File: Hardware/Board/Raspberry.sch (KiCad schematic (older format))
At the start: 5 parts

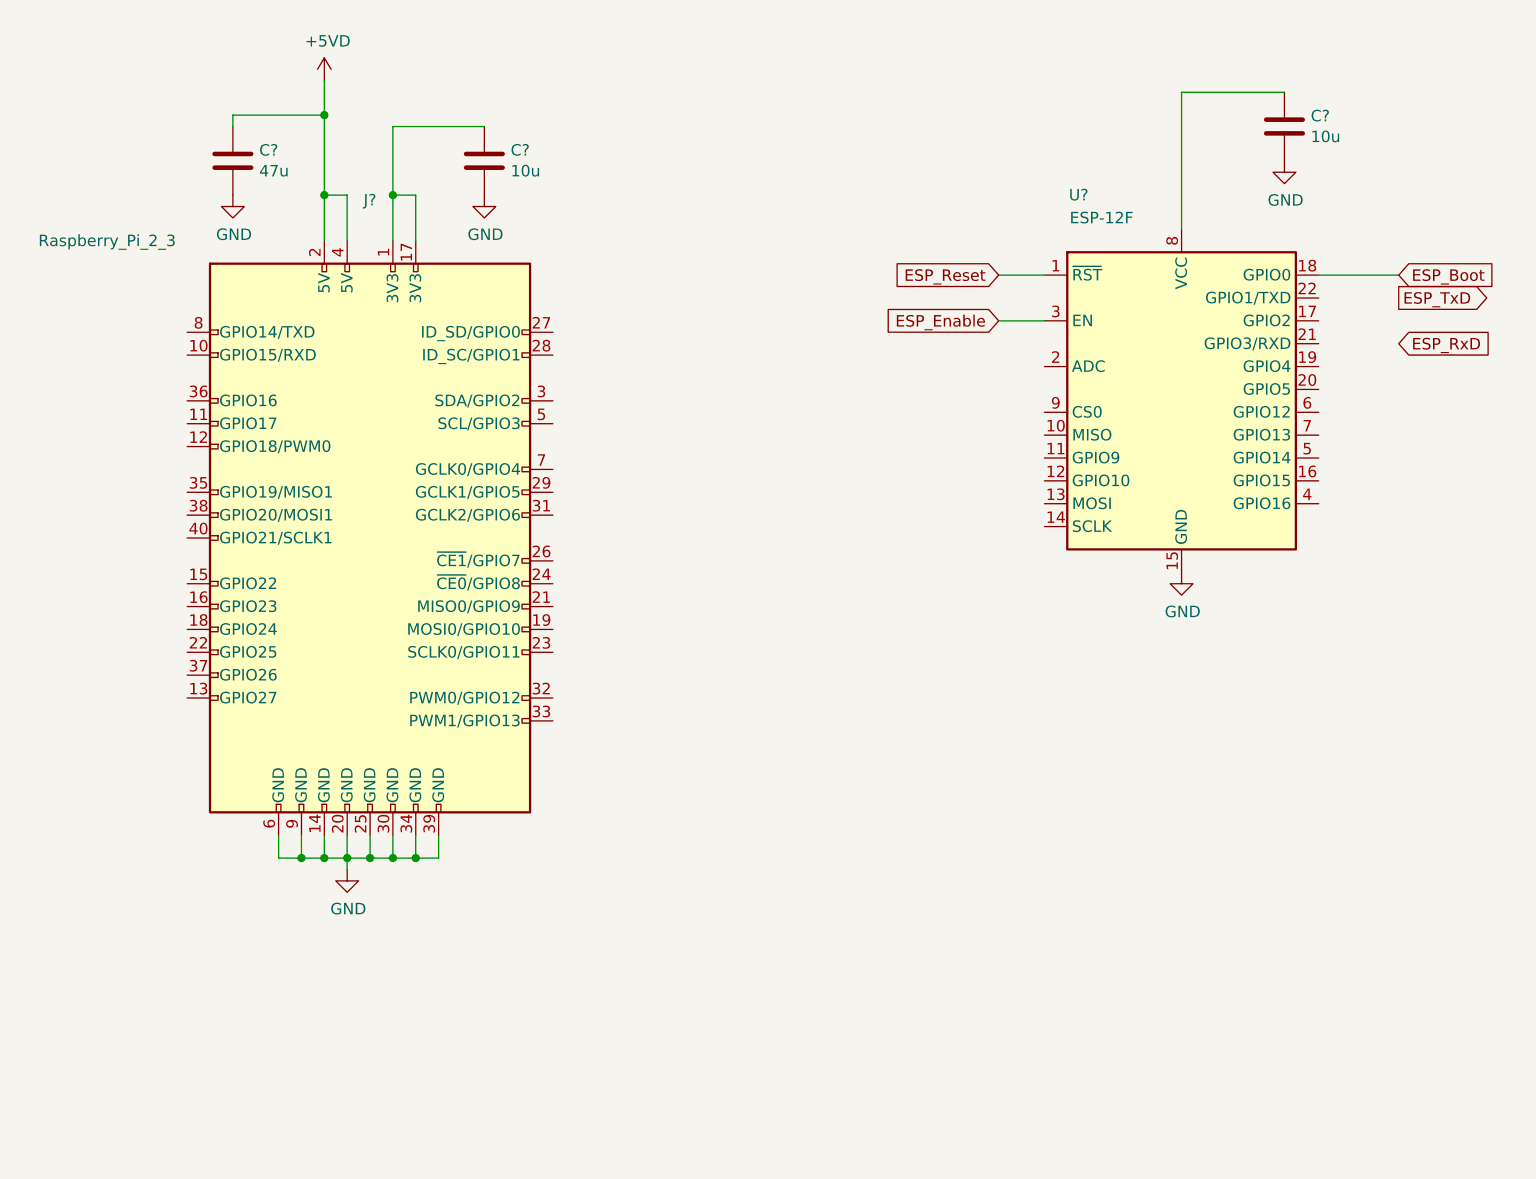
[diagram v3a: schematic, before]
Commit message: Netzliste und Board erstellt, hier sind noch Fehler im Bereich Footprints, BLE Modul nRF8001 hinzugefügt, erste Anschlussklemmen zugefügt
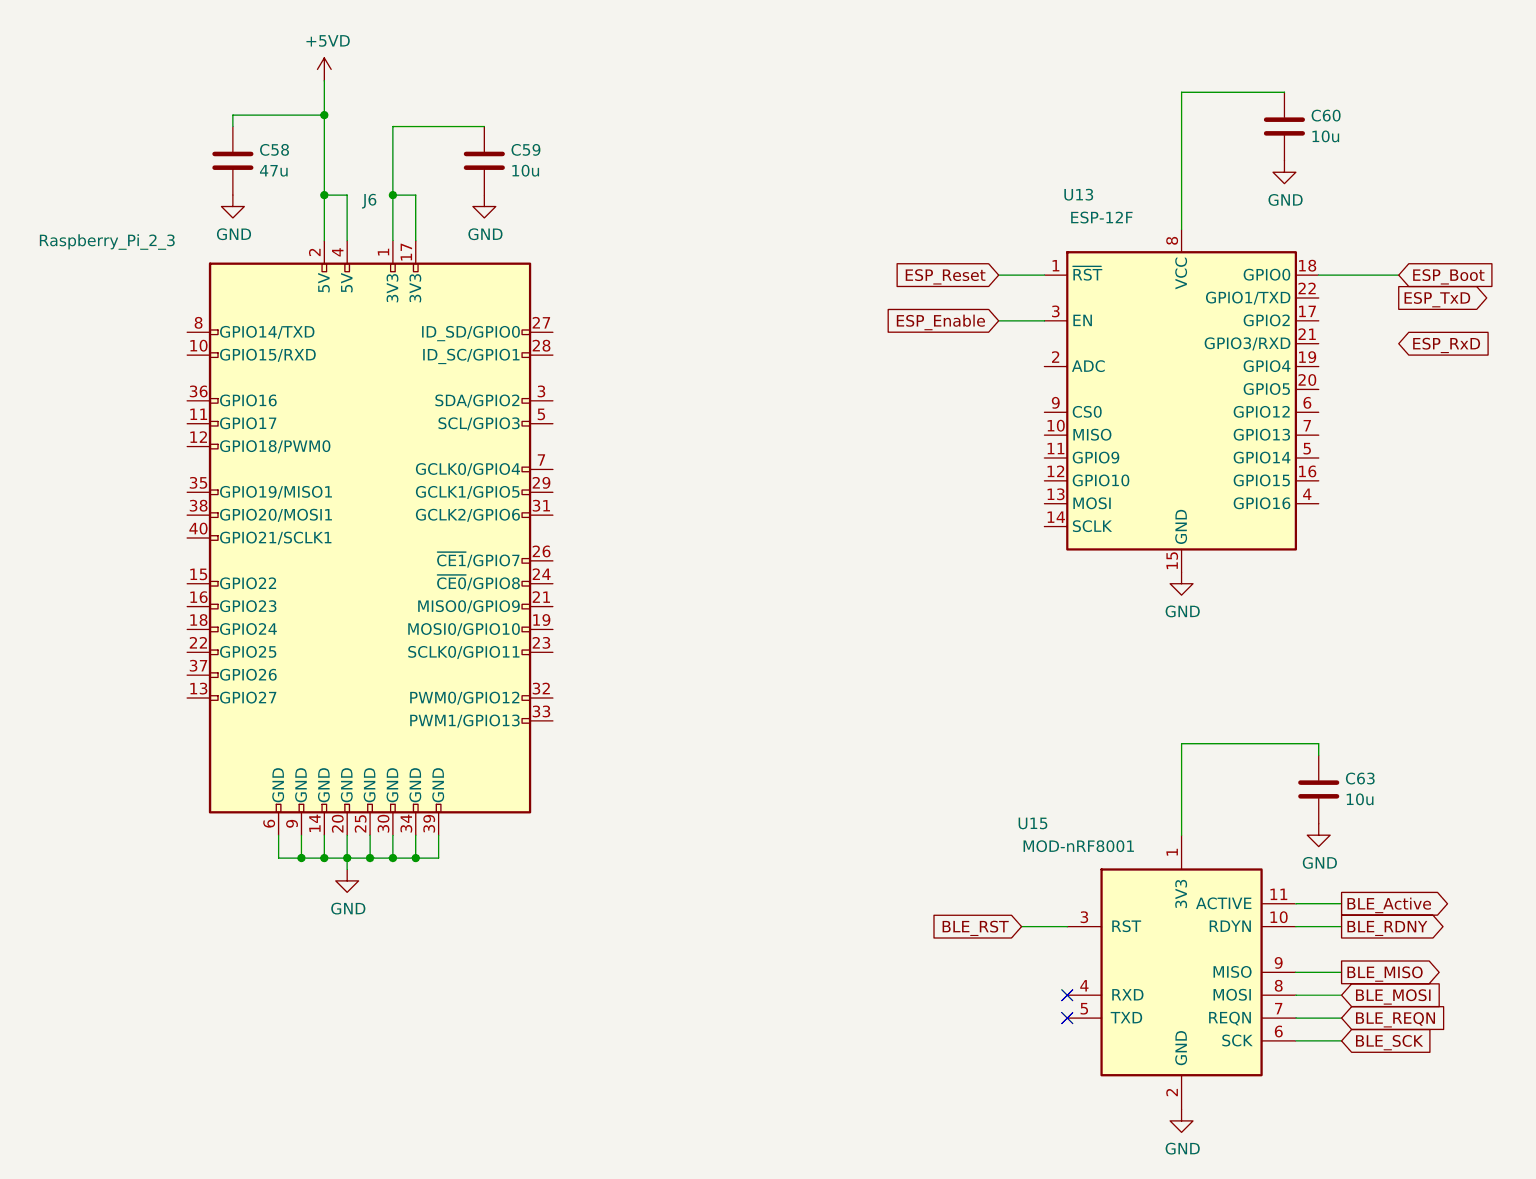
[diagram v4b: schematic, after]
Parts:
- added C63: 10u, Capacitor_SMD:C_1210_3225Metric, symbol Device:C
- added U15: MOD-nRF8001, RF_Module:MOD-nRF8001, symbol RF_Bluetooth:MOD-nRF8001
- C58, C59, C60: renamed from C?; footprint (none) -> Capacitor_SMD:C_1210_3225Metric
- J6: renamed from J?; footprint (none) -> Connector_IDC:IDC-Header_2x20_P2.54mm_Vertical
- gave numbers to parts that had none: 1
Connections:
- net GND: now also C63.2, U15.2 (GND)
- new net: C63.1, U15.1 (3V3)
- new net BLE_Active: U15.11 (ACTIVE)
- new net BLE_MISO: U15.9 (MISO)
- new net BLE_MOSI: U15.8 (MOSI)
- new net BLE_RDNY: U15.10 (RDYN)
- new net BLE_REQN: U15.7 (REQN)
- new net BLE_RST: U15.3 (RST)
- new net BLE_SCK: U15.6 (SCK)
- no-connect marks 0 -> 2
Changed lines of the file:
@@
 $EndDescr
 $Comp
-L Connector:Raspberry_Pi_2_3 J?
+L Connector:Raspberry_Pi_2_3 J6
 U 1 1 5C8BC8C5
 P 4400 3300
-F 0 "J?" H 4400 4778 50  0000 C CNN
+F 0 "J6" H 4400 4778 50  0000 C CNN
 F 1 "Raspberry_Pi_2_3" H 3250 4600 50  0000 C CNN
-F 2 "" H 4400 3300 50  0001 C CNN
+F 2 "Connector_IDC:IDC-Header_2x20_P2.54mm_Vertical" H 4400 3300 50  0001 C CNN
 F 3 "https://www.raspberrypi.org/documentation/hardware/raspberrypi/schematics/rpi_SCH_3bplus_1p0_reduced.pdf" H 4400 3300 50  0001 C CNN
 	1    4400 3300
@@
 $EndComp
 $Comp
-L power:GND #PWR?
+L power:GND #PWR0229
 U 1 1 5CC01696
 P 4300 4750
-F 0 "#PWR?" H 4300 4500 50  0001 C CNN
+F 0 "#PWR0229" H 4300 4500 50  0001 C CNN
 F 1 "GND" H 4305 4577 50  0000 C CNN
 F 2 "" H 4300 4750 50  0001 C CNN
@@
 	4600 4700 4500 4700
 $Comp
-L power:+5VD #PWR?
+L power:+5VD #PWR0230
 U 1 1 5CC0193E
 P 4200 1300
-F 0 "#PWR?" H 4200 1150 50  0001 C CNN
+F 0 "#PWR0230" H 4200 1150 50  0001 C CNN
 F 1 "+5VD" H 4215 1473 50  0000 C CNN
 F 2 "" H 4200 1300 50  0001 C CNN
@@
 $EndComp
 $Comp
-L Device:C C?
+L Device:C C58
 U 1 1 5CC01965
 P 3800 1650
-F 0 "C?" H 3915 1696 50  0000 L CNN
+F 0 "C58" H 3915 1696 50  0000 L CNN
 F 1 "47u" H 3915 1605 50  0000 L CNN
-F 2 "" H 3838 1500 50  0001 C CNN
+F 2 "Capacitor_SMD:C_1210_3225Metric" H 3838 1500 50  0001 C CNN
 F 3 "~" H 3800 1650 50  0001 C CNN
 	1    3800 1650
@@
 $EndComp
 $Comp
-L Device:C C?
+L Device:C C59
 U 1 1 5CC019EB
 P 4900 1650
-F 0 "C?" H 5015 1696 50  0000 L CNN
+F 0 "C59" H 5015 1696 50  0000 L CNN
 F 1 "10u" H 5015 1605 50  0000 L CNN
-F 2 "" H 4938 1500 50  0001 C CNN
+F 2 "Capacitor_SMD:C_1210_3225Metric" H 4938 1500 50  0001 C CNN
 F 3 "~" H 4900 1650 50  0001 C CNN
 	1    4900 1650
@@
 $EndComp
 $Comp
-L power:GND #PWR?
+L power:GND #PWR0231
 U 1 1 5CC01A3B
 P 3800 1800
-F 0 "#PWR?" H 3800 1550 50  0001 C CNN
+F 0 "#PWR0231" H 3800 1550 50  0001 C CNN
 F 1 "GND" H 3805 1627 50  0000 C CNN
 F 2 "" H 3800 1800 50  0001 C CNN
@@
 $EndComp
 $Comp
-L power:GND #PWR?
+L power:GND #PWR0232
 U 1 1 5CC01B10
 P 4900 1800
-F 0 "#PWR?" H 4900 1550 50  0001 C CNN
+F 0 "#PWR0232" H 4900 1550 50  0001 C CNN
 F 1 "GND" H 4905 1627 50  0000 C CNN
 F 2 "" H 4900 1800 50  0001 C CNN
@@
 	4200 1450 4200 1300
 $Comp
-L RF_Module:ESP-12F U?
+L RF_Module:ESP-12F U13
 U 1 1 5CAB8BB3
 P 7950 2750
-F 0 "U?" H 7500 3700 50  0000 C CNN
+F 0 "U13" H 7500 3700 50  0000 C CNN
 F 1 "ESP-12F" H 7600 3600 50  0000 C CNN
 F 2 "RF_Module:ESP-12E" H 7950 2750 50  0001 C CNN
@@
 ESP_Enable
 $Comp
-L Device:C C?
+L Device:C C60
 U 1 1 5CB2F4A7
 P 8400 1500
-F 0 "C?" H 8515 1546 50  0000 L CNN
+F 0 "C60" H 8515 1546 50  0000 L CNN
 F 1 "10u" H 8515 1455 50  0000 L CNN
-F 2 "" H 8438 1350 50  0001 C CNN
+F 2 "Capacitor_SMD:C_1210_3225Metric" H 8438 1350 50  0001 C CNN
 F 3 "~" H 8400 1500 50  0001 C CNN
 	1    8400 1500
@@
 $EndComp
 $Comp
-L power:GND #PWR?
+L power:GND #PWR0233
 U 1 1 5CB2F4AE
 P 8400 1650
-F 0 "#PWR?" H 8400 1400 50  0001 C CNN
+F 0 "#PWR0233" H 8400 1400 50  0001 C CNN
 F 1 "GND" H 8405 1477 50  0000 C CNN
 F 2 "" H 8400 1650 50  0001 C CNN
@@
 $EndComp
 $Comp
-L power:GND #PWR?
+L power:GND #PWR0234
 U 1 1 5CB2F86B
 P 7950 3450
-F 0 "#PWR?" H 7950 3200 50  0001 C CNN
+F 0 "#PWR0234" H 7950 3200 50  0001 C CNN
 F 1 "GND" H 7955 3277 50  0000 C CNN
 F 2 "" H 7950 3450 50  0001 C CNN
@@
 Wire Wire Line
 	7950 1350 8400 1350
+$Comp
+L RF_Bluetooth:MOD-nRF8001 U15
+U 1 1 5CDFE053
+P 7950 5200
+F 0 "U15" H 7300 5850 50  0000 C CNN
+F 1 "MOD-nRF8001" H 7500 5750 50  0000 C CNN
+F 2 "RF_Module:MOD-nRF8001" H 8000 5250 50  0001 C CNN
+F 3 "https://www.olimex.com/Products/Modules/RF/MOD-nRF8001/" H 8000 5200 50  0001 C CNN
+	1    7950 5200
+	1    0    0    -1
+$EndComp
+Text GLabel 8650 5300 2    50   Input ~ 0
+BLE_MOSI
+Text GLabel 8650 5500 2    50   Input ~ 0
+BLE_SCK
+Text GLabel 8650 5200 2    50   Output ~ 0
+BLE_MISO
+$Comp
+L power:GND #PWR0249
+U 1 1 5CDFE14F
+P 7950 5800
+F 0 "#PWR0249" H 7950 5550 50  0001 C CNN
+F 1 "GND" H 7955 5627 50  0000 C CNN
+F 2 "" H 7950 5800 50  0001 C CNN
+F 3 "" H 7950 5800 50  0001 C CNN
+	1    7950 5800
+	1    0    0    -1
+$EndComp
+$Comp
+L Device:C C63
+U 1 1 5CDFE647
+P 8550 4400
+F 0 "C63" H 8665 4446 50  0000 L CNN
+F 1 "10u" H 8665 4355 50  0000 L CNN
+F 2 "Capacitor_SMD:C_1210_3225Metric" H 8588 4250 50  0001 C CNN
+F 3 "~" H 8550 4400 50  0001 C CNN
+	1    8550 4400
+	1    0    0    -1
+$EndComp
+$Comp
+L power:GND #PWR0250
+U 1 1 5CDFE64E
+P 8550 4550
+F 0 "#PWR0250" H 8550 4300 50  0001 C CNN
+F 1 "GND" H 8555 4377 50  0000 C CNN
+F 2 "" H 8550 4550 50  0001 C CNN
+F 3 "" H 8550 4550 50  0001 C CNN
+	1    8550 4550
+	1    0    0    -1
+$EndComp
+Wire Wire Line
+	8550 4250 8550 4200
+Wire Wire Line
+	8550 4200 7950 4200
+Wire Wire Line
+	7950 4200 7950 4600
+NoConn ~ 7450 5300
+NoConn ~ 7450 5400
+Text GLabel 8650 5400 2    50   Input ~ 0
+BLE_REQN
+Text GLabel 8650 5000 2    50   Output ~ 0
+BLE_RDNY
+Text GLabel 8650 4900 2    50   Output ~ 0
+BLE_Active
+Text GLabel 7250 5000 0    50   Input ~ 0
+BLE_RST
+Wire Wire Line
+	7250 5000 7450 5000
+Wire Wire Line
+	8450 4900 8650 4900
+Wire Wire Line
+	8450 5000 8650 5000
+Wire Wire Line
+	8450 5200 8650 5200
+Wire Wire Line
+	8450 5300 8650 5300
+Wire Wire Line
+	8450 5400 8650 5400
+Wire Wire Line
+	8450 5500 8650 5500
 $EndSCHEMATC

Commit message: Eine Menge Arbeit auf der GPN, fast fertig im Schaltplan.
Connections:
- net UART4_TX: now reaches J6.10 (GPIO15/RXD)
- net Rasp_Shutdown: now reaches J6.27 (ID_SD/GPIO0)
- net Rasp_down: now reaches J6.28 (ID_SC/GPIO1)
- net UART4_RX: now reaches J6.8 (GPIO14/TXD)
- net UART5_TX: now reaches U13.21 (GPIO3/RXD)
- net UART5_RX: now reaches U13.22 (GPIO1/TXD)
- net +3.3VA: now reaches C60.1, U13.8 (VCC)
- net +3.3VA: now also C63.1, U15.1 (3V3)
- net BLE_MISO renamed SPI1_MISO
- net BLE_MOSI renamed SPI1_MOSI
- net BLE_RDNY renamed BLE_INT
- net BLE_REQN renamed SPI1_NSS
- net BLE_SCK renamed SPI1_SCK
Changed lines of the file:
@@
 EESchema Schematic File Version 4
 LIBS:Womo-cache
-EELAYER 26 0
+EELAYER 29 0
 EELAYER END
 $Descr A4 11693 8268
@@
 	1    0    0    -1
 $EndComp
-Text GLabel 8900 2150 2    50   Input ~ 0
-ESP_Boot
-Text GLabel 8900 2250 2    50   Output ~ 0
-ESP_TxD
-Text GLabel 8900 2450 2    50   Input ~ 0
-ESP_RxD
 Text GLabel 7150 2150 0    50   Input ~ 0
 ESP_Reset
@@
 	7150 2350 7350 2350
 Wire Wire Line
-	8550 2150 8900 2150
-Wire Wire Line
 	7950 1950 7950 1350
 Wire Wire Line
@@
 $EndComp
 Text GLabel 8650 5300 2    50   Input ~ 0
-BLE_MOSI
+SPI1_MOSI
 Text GLabel 8650 5500 2    50   Input ~ 0
-BLE_SCK
+SPI1_SCK
 Text GLabel 8650 5200 2    50   Output ~ 0
-BLE_MISO
+SPI1_MISO
 $Comp
 L power:GND #PWR0249
@@
 NoConn ~ 7450 5400
 Text GLabel 8650 5400 2    50   Input ~ 0
-BLE_REQN
+SPI1_NSS
 Text GLabel 8650 5000 2    50   Output ~ 0
-BLE_RDNY
+BLE_INT
 Text GLabel 8650 4900 2    50   Output ~ 0
 BLE_Active
@@
 Wire Wire Line
 	8450 5500 8650 5500
+Text GLabel 8700 2450 2    50   Output ~ 0
+UART5_TX
+Text GLabel 3500 2500 0    50   Input ~ 0
+UART4_TX
+Text GLabel 3500 2400 0    50   Output ~ 0
+UART4_RX
+Text GLabel 8700 2250 2    50   Output ~ 0
+UART5_RX
+Text GLabel 8700 2150 2    50   Input ~ 0
+ESP_Boot
+Wire Wire Line
+	8700 2150 8550 2150
+Wire Wire Line
+	8700 2250 8550 2250
+Wire Wire Line
+	8700 2450 8550 2450
+Wire Wire Line
+	3600 2400 3500 2400
+Wire Wire Line
+	3600 2500 3500 2500
+Text GLabel 5300 2400 2    50   Input ~ 0
+Rasp_Shutdown
+Text GLabel 5300 2500 2    50   Output ~ 0
+Rasp_down
+Wire Wire Line
+	5300 2400 5200 2400
+Wire Wire Line
+	5300 2500 5200 2500
+$Comp
+L power:+3.3VA #PWR?
+U 1 1 5D4E449C
+P 7950 4100
+AR Path="/5C8BBC9A/5D4E449C" Ref="#PWR?"  Part="1"
+AR Path="/5E0C5EEA/5D4E449C" Ref="#PWR?"  Part="1"
+F 0 "#PWR?" H 7950 3950 50  0001 C CNN
+F 1 "+3.3VA" H 7965 4273 50  0000 C CNN
+F 2 "" H 7950 4100 50  0001 C CNN
+F 3 "" H 7950 4100 50  0001 C CNN
+	1    7950 4100
+	1    0    0    -1
+$EndComp
+Wire Wire Line
+	7950 4100 7950 4200
+Connection ~ 7950 4200
+$Comp
+L power:+3.3VA #PWR?
+U 1 1 5D4E6269
+P 7950 1250
+AR Path="/5C8BBC9A/5D4E6269" Ref="#PWR?"  Part="1"
+AR Path="/5E0C5EEA/5D4E6269" Ref="#PWR?"  Part="1"
+F 0 "#PWR?" H 7950 1100 50  0001 C CNN
+F 1 "+3.3VA" H 7965 1423 50  0000 C CNN
+F 2 "" H 7950 1250 50  0001 C CNN
+F 3 "" H 7950 1250 50  0001 C CNN
+	1    7950 1250
+	1    0    0    -1
+$EndComp
+Wire Wire Line
+	7950 1250 7950 1350
+Connection ~ 7950 1350
 $EndSCHEMATC

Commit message: Board to Board Verbindung eingefügt
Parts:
- removed C63: 10u, Capacitor_SMD:C_1210_3225Metric, symbol Device:C
- removed U15: MOD-nRF8001, RF_Module:MOD-nRF8001, symbol RF_Bluetooth:MOD-nRF8001
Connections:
- no-connect marks 2 -> 0
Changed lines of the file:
@@
 EESchema Schematic File Version 4
 LIBS:Womo-cache
-EELAYER 29 0
+EELAYER 26 0
 EELAYER END
 $Descr A4 11693 8268
@@
 Wire Wire Line
 	7950 1350 8400 1350
-$Comp
-L RF_Bluetooth:MOD-nRF8001 U15
-U 1 1 5CDFE053
-P 7950 5200
-F 0 "U15" H 7300 5850 50  0000 C CNN
-F 1 "MOD-nRF8001" H 7500 5750 50  0000 C CNN
-F 2 "RF_Module:MOD-nRF8001" H 8000 5250 50  0001 C CNN
-F 3 "https://www.olimex.com/Products/Modules/RF/MOD-nRF8001/" H 8000 5200 50  0001 C CNN
-	1    7950 5200
-	1    0    0    -1
-$EndComp
-Text GLabel 8650 5300 2    50   Input ~ 0
-SPI1_MOSI
-Text GLabel 8650 5500 2    50   Input ~ 0
-SPI1_SCK
-Text GLabel 8650 5200 2    50   Output ~ 0
-SPI1_MISO
-$Comp
-L power:GND #PWR0249
-U 1 1 5CDFE14F
-P 7950 5800
-F 0 "#PWR0249" H 7950 5550 50  0001 C CNN
-F 1 "GND" H 7955 5627 50  0000 C CNN
-F 2 "" H 7950 5800 50  0001 C CNN
-F 3 "" H 7950 5800 50  0001 C CNN
-	1    7950 5800
-	1    0    0    -1
-$EndComp
-$Comp
-L Device:C C63
-U 1 1 5CDFE647
-P 8550 4400
-F 0 "C63" H 8665 4446 50  0000 L CNN
-F 1 "10u" H 8665 4355 50  0000 L CNN
-F 2 "Capacitor_SMD:C_1210_3225Metric" H 8588 4250 50  0001 C CNN
-F 3 "~" H 8550 4400 50  0001 C CNN
-	1    8550 4400
-	1    0    0    -1
-$EndComp
-$Comp
-L power:GND #PWR0250
-U 1 1 5CDFE64E
-P 8550 4550
-F 0 "#PWR0250" H 8550 4300 50  0001 C CNN
-F 1 "GND" H 8555 4377 50  0000 C CNN
-F 2 "" H 8550 4550 50  0001 C CNN
-F 3 "" H 8550 4550 50  0001 C CNN
-	1    8550 4550
-	1    0    0    -1
-$EndComp
-Wire Wire Line
-	8550 4250 8550 4200
-Wire Wire Line
-	8550 4200 7950 4200
-Wire Wire Line
-	7950 4200 7950 4600
-NoConn ~ 7450 5300
-NoConn ~ 7450 5400
-Text GLabel 8650 5400 2    50   Input ~ 0
-SPI1_NSS
-Text GLabel 8650 5000 2    50   Output ~ 0
-BLE_INT
-Text GLabel 8650 4900 2    50   Output ~ 0
-BLE_Active
-Text GLabel 7250 5000 0    50   Input ~ 0
-BLE_RST
-Wire Wire Line
-	7250 5000 7450 5000
-Wire Wire Line
-	8450 4900 8650 4900
-Wire Wire Line
-	8450 5000 8650 5000
-Wire Wire Line
-	8450 5200 8650 5200
-Wire Wire Line
-	8450 5300 8650 5300
-Wire Wire Line
-	8450 5400 8650 5400
-Wire Wire Line
-	8450 5500 8650 5500
 Text GLabel 8700 2450 2    50   Output ~ 0
 UART5_TX
@@
 $Comp
 L power:+3.3VA #PWR?
-U 1 1 5D4E449C
-P 7950 4100
-AR Path="/5C8BBC9A/5D4E449C" Ref="#PWR?"  Part="1"
-AR Path="/5E0C5EEA/5D4E449C" Ref="#PWR?"  Part="1"
-F 0 "#PWR?" H 7950 3950 50  0001 C CNN
-F 1 "+3.3VA" H 7965 4273 50  0000 C CNN
-F 2 "" H 7950 4100 50  0001 C CNN
-F 3 "" H 7950 4100 50  0001 C CNN
-	1    7950 4100
-	1    0    0    -1
-$EndComp
-Wire Wire Line
-	7950 4100 7950 4200
-Connection ~ 7950 4200
-$Comp
-L power:+3.3VA #PWR?
 U 1 1 5D4E6269
 P 7950 1250
 AR Path="/5C8BBC9A/5D4E6269" Ref="#PWR?"  Part="1"
 AR Path="/5E0C5EEA/5D4E6269" Ref="#PWR?"  Part="1"
-F 0 "#PWR?" H 7950 1100 50  0001 C CNN
+AR Path="/5C8BC88B/5D4E6269" Ref="#PWR0254"  Part="1"
+F 0 "#PWR0254" H 7950 1100 50  0001 C CNN
 F 1 "+3.3VA" H 7965 1423 50  0000 C CNN
 F 2 "" H 7950 1250 50  0001 C CNN
